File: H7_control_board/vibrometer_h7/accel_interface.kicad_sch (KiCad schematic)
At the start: 0 parts

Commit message: added cubeIDE projects
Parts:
- added C301, C302: 100n, symbol Device:C
- added D301: LED, symbol Device:LED
- added J301, J302: Conn_01x08_Socket, symbol Connector:Conn_01x08_Socket
- added R302: 0R, symbol Device:R_Small_US
- added R?: R, symbol Device:R_Small_US
- added XL1: LSM6DS3, Package_LGA:LGA-14_3x2.5mm_P0.5mm_LayoutBorder3x4y, symbol Sensor_Motion:LSM6DS3
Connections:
- new net: D301.1 (K), R?.1
- new net: D301.2 (A), R302.2
- new net +3V3: C301.1, C302.1, J302.8 (Pin_8), R302.1, XL1.5 (VDDIO), XL1.8 (VDD)
- new net GND: C301.2, C302.2, J302.1 (Pin_1), R?.2, XL1.6 (GND), XL1.7 (GND)
- new net SPI_3V3: J301.8 (Pin_8)
- new net SPI_CS: J301.2 (Pin_2), J302.2 (Pin_2), XL1.12 (CS)
- new net SPI_GND: J301.1 (Pin_1)
- new net SPI_INT1: J301.7 (Pin_7), J302.7 (Pin_7), XL1.4 (INT1)
- new net SPI_INT2: J301.6 (Pin_6), J302.6 (Pin_6), XL1.9 (INT2)
- new net SPI_MISO: J301.5 (Pin_5), J302.5 (Pin_5), XL1.1 (SDO/SA0)
- new net SPI_MOSI: J301.4 (Pin_4), J302.4 (Pin_4), XL1.14 (SDA)
- new net SPI_SCLK: J301.3 (Pin_3), J302.3 (Pin_3), XL1.13 (SCL)
- no-connect marks 0 -> 2

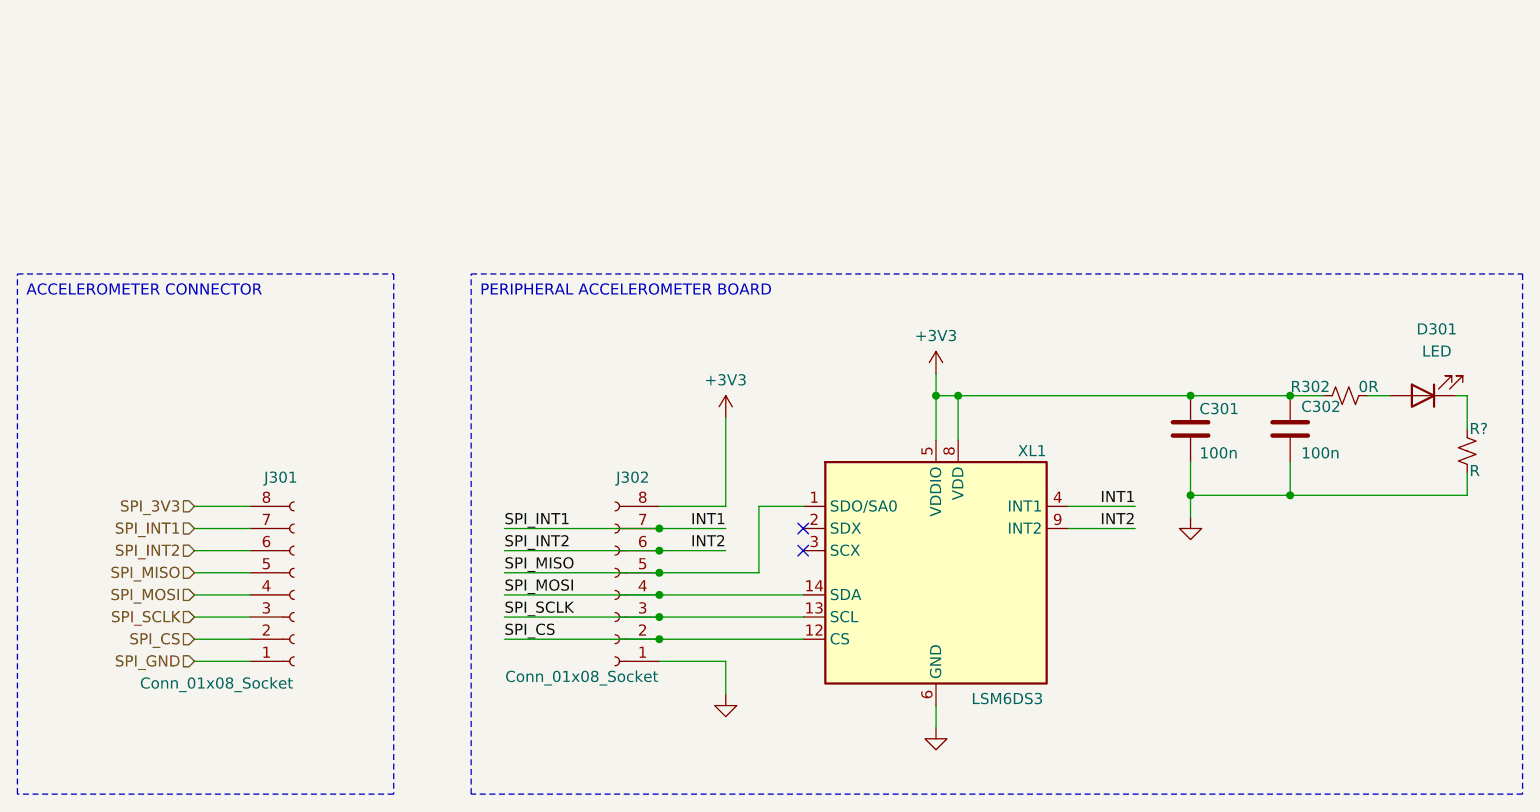
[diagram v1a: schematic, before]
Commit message: added bus notation to kicad schematic
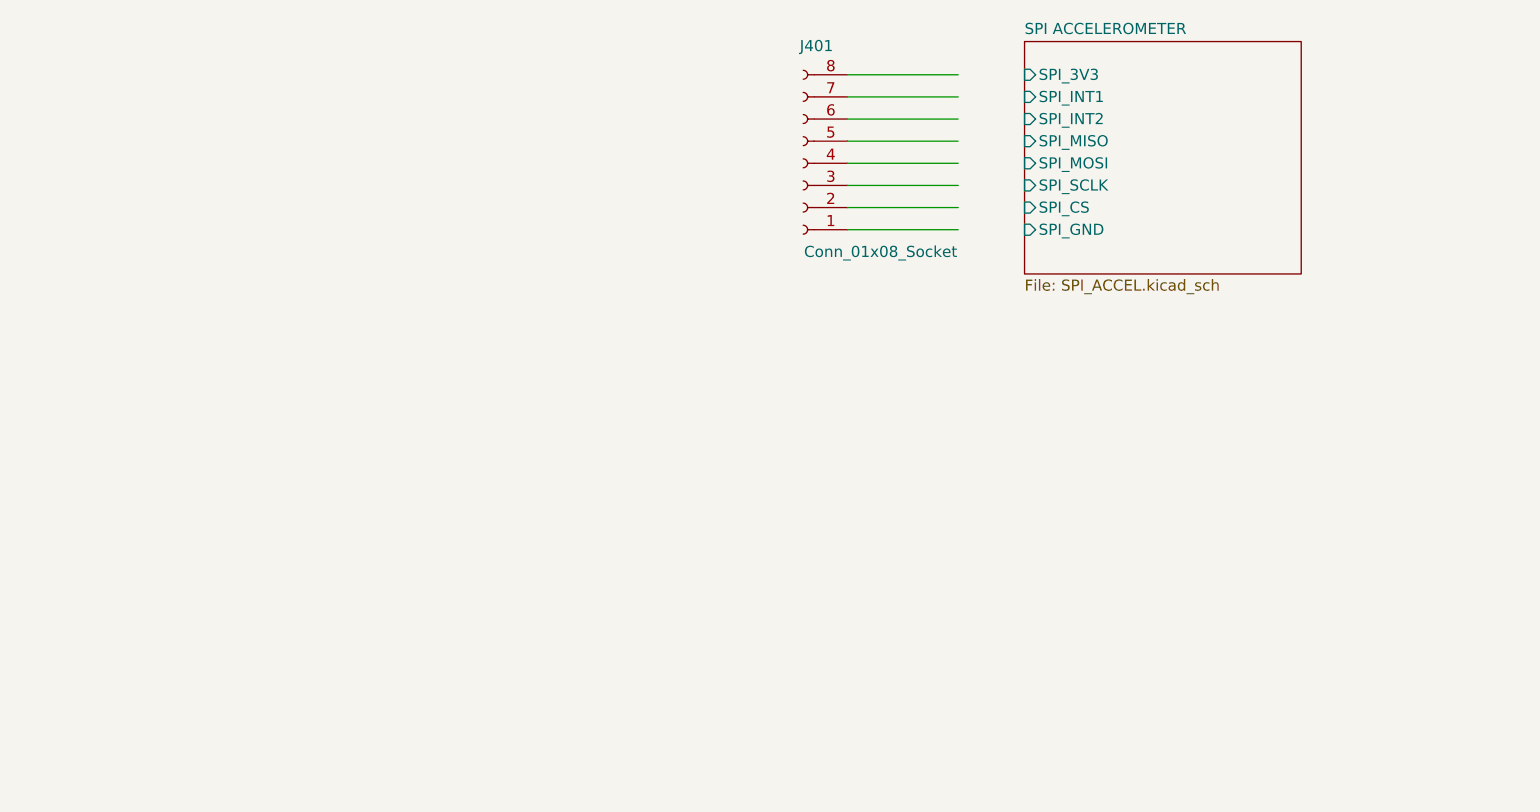
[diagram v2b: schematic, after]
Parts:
- removed C301, C302: 100n, symbol Device:C
- removed D301: LED, symbol Device:LED
- removed J301, J302: Conn_01x08_Socket, symbol Connector:Conn_01x08_Socket
- removed R302: 0R, symbol Device:R_Small_US
- removed R?: R, symbol Device:R_Small_US
- removed XL1: LSM6DS3, Package_LGA:LGA-14_3x2.5mm_P0.5mm_LayoutBorder3x4y, symbol Sensor_Motion:LSM6DS3
- added J401: Conn_01x08_Socket, symbol Connector:Conn_01x08_Socket
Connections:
- no-connect marks 2 -> 0
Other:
- added sheet SPI ACCELEROMETER (SPI_ACCEL.kicad_sch)

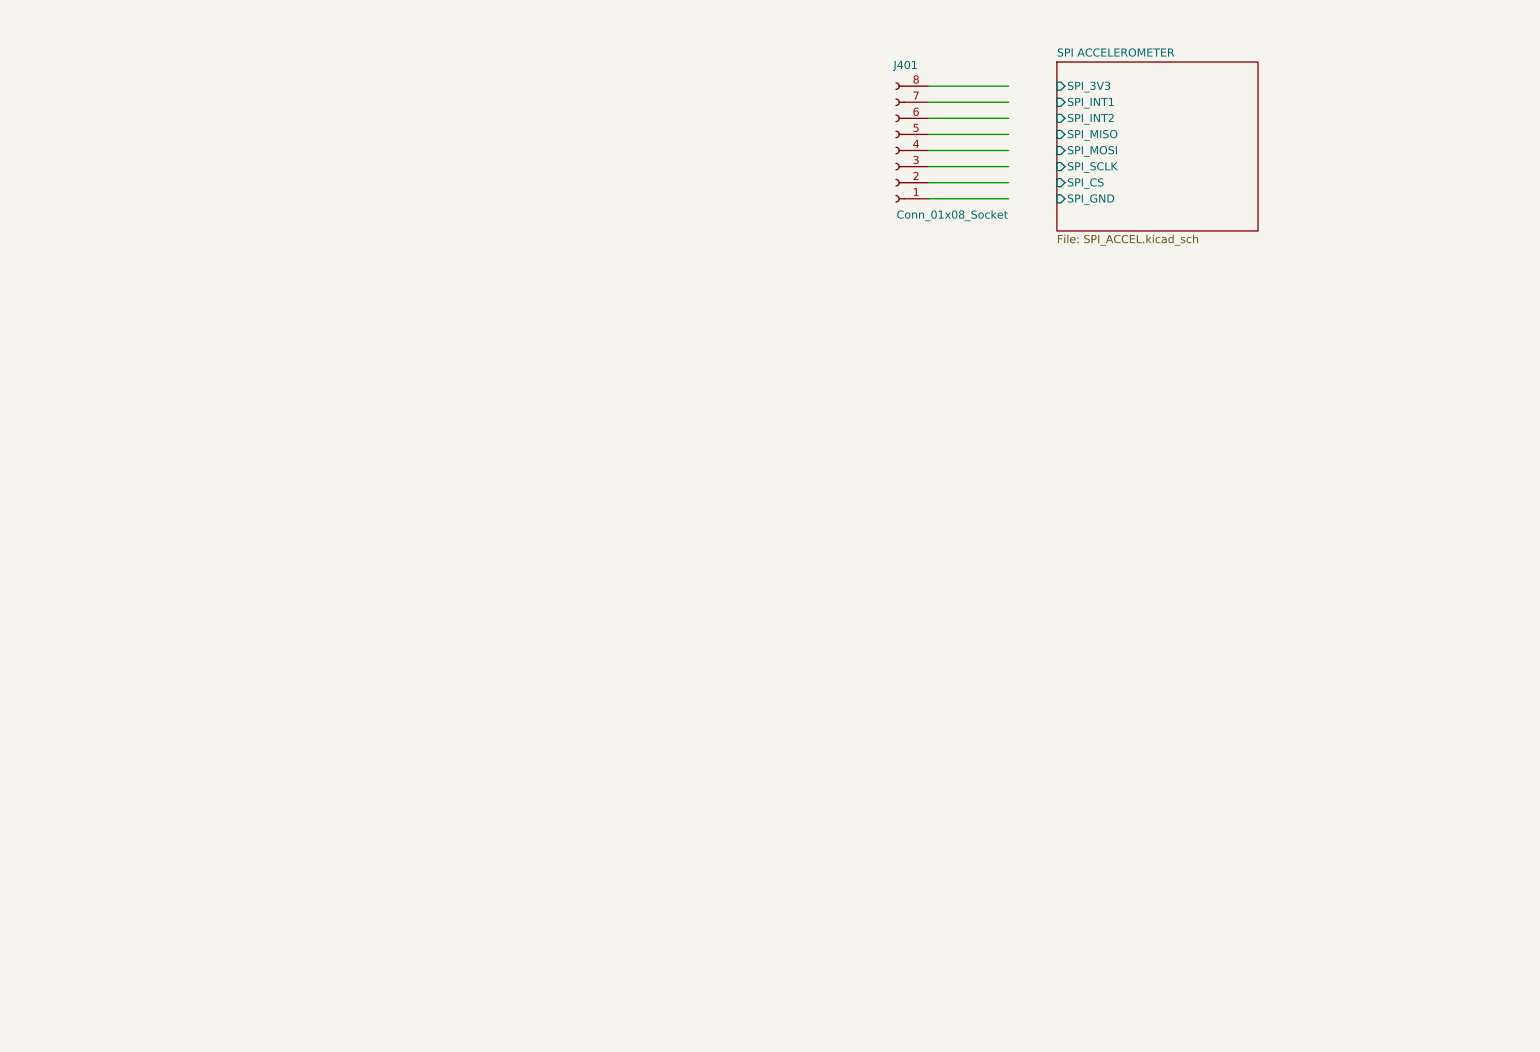
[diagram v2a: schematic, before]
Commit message: added UI leds to schematic
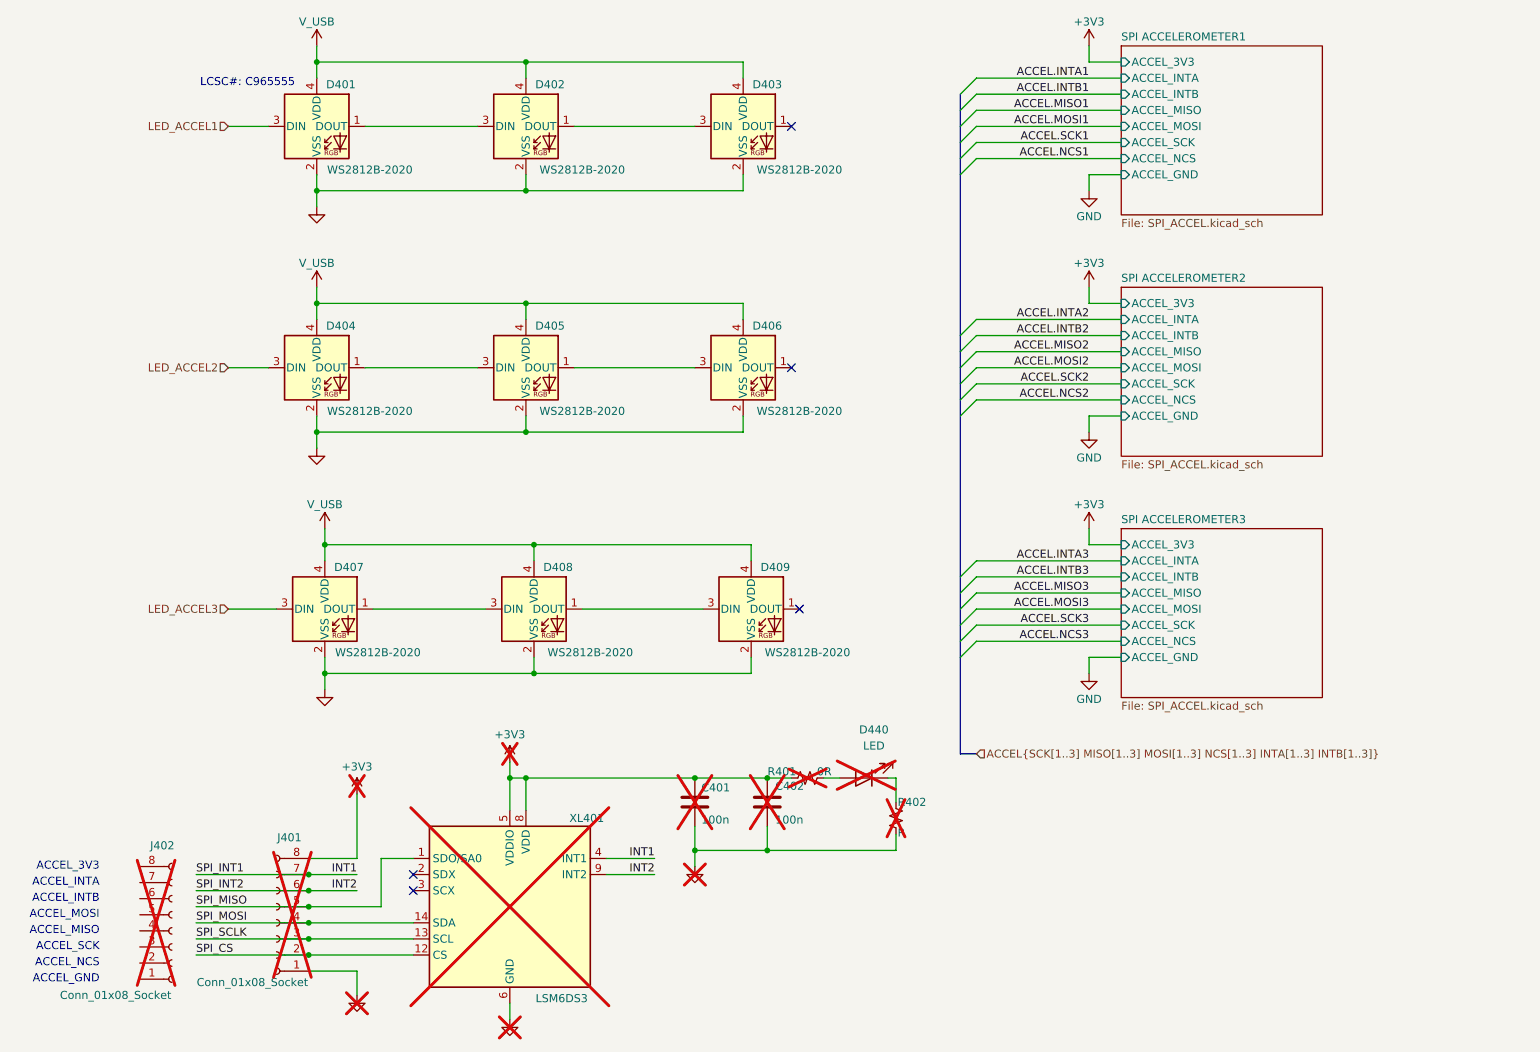
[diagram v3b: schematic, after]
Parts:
- added C401, C402: 100n, symbol Device:C
- added D401, D402, D403, D404, D405, D406, D407, D408, D409: WS2812B-2020, LED_SMD:LED_WS2812B-2020_PLCC4_2.0x2.0mm, symbol LED:WS2812B-2020
- added D440: LED, symbol Device:LED
- added J402: Conn_01x08_Socket, symbol Connector:Conn_01x08_Socket
- added R401: 0R, symbol Device:R_Small_US
- added R402: R, symbol Device:R_Small_US
- added XL401: LSM6DS3, Package_LGA:LGA-14_3x2.5mm_P0.5mm_LayoutBorder3x4y, symbol Sensor_Motion:LSM6DS3
- J401: now not fitted
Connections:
- net GND: now reaches J401.1 (Pin_1)
- net GND: now also C401.2, C402.2, D401.2 (VSS), D402.2 (VSS), D403.2 (VSS), D404.2 (VSS), D405.2 (VSS), D406.2 (VSS), D407.2 (VSS), D408.2 (VSS), D409.2 (VSS), R402.2, XL401.6 (GND), XL401.7 (GND)
- net SPI_CS: now reaches J401.2 (Pin_2)
- net SPI_CS: now also XL401.12 (CS)
- net SPI_SCLK: now reaches J401.3 (Pin_3)
- net SPI_SCLK: now also XL401.13 (SCL)
- net SPI_MOSI: now reaches J401.4 (Pin_4)
- net SPI_MOSI: now also XL401.14 (SDA)
- net SPI_MISO: now reaches J401.5 (Pin_5)
- net SPI_MISO: now also XL401.1 (SDO/SA0)
- net INT2: now reaches J401.6 (Pin_6)
- net INT2: now also XL401.9 (INT2)
- net INT1: now reaches J401.7 (Pin_7)
- net INT1: now also XL401.4 (INT1)
- net +3V3: now reaches J401.8 (Pin_8)
- net +3V3: now also C401.1, C402.1, R401.1, XL401.5 (VDDIO), XL401.8 (VDD)
- new net: D402.1 (DOUT), D403.3 (DIN)
- new net: D401.1 (DOUT), D402.3 (DIN)
- new net: D405.1 (DOUT), D406.3 (DIN)
- new net: D440.1 (K), R402.1
- new net: D440.2 (A), R401.2
- new net: D408.1 (DOUT), D409.3 (DIN)
- new net: D407.1 (DOUT), D408.3 (DIN)
- new net: D404.1 (DOUT), D405.3 (DIN)
- new net LED_ACCEL1: D401.3 (DIN)
- new net LED_ACCEL2: D404.3 (DIN)
- new net LED_ACCEL3: D407.3 (DIN)
- new net V_USB: D401.4 (VDD), D402.4 (VDD), D403.4 (VDD), D404.4 (VDD), D405.4 (VDD), D406.4 (VDD), D407.4 (VDD), D408.4 (VDD), D409.4 (VDD)
- no-connect marks 0 -> 5
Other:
- sheet SPI ACCELEROMETER renamed SPI ACCELEROMETER1
- added sheet SPI ACCELEROMETER2 (SPI_ACCEL.kicad_sch)
- added sheet SPI ACCELEROMETER3 (SPI_ACCEL.kicad_sch)
- sheet SPI ACCELEROMETER1 ports: added ACCEL_3V3, ACCEL_GND, ACCEL_INTA, ACCEL_INTB, ACCEL_MISO, ACCEL_MOSI, ACCEL_NCS, ACCEL_SCK; removed SPI_3V3, SPI_CS, SPI_GND, SPI_INT1, SPI_INT2, SPI_MISO, SPI_MOSI, SPI_SCLK
- note added: "ACCEL_3V3"
- note added: "ACCEL_GND"
- note added: "ACCEL_INTA"
- note added: "ACCEL_INTB"
- note added: "ACCEL_MISO"
- note added: "ACCEL_MOSI"
- note added: "ACCEL_NCS"
- note added: "ACCEL_SCK"
- note added: "LCSC#: C965555"

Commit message: working on getting ERC to run... almost there!
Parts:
- removed C401, C402: 100n, symbol Device:C
- removed D440: LED, symbol Device:LED
- removed J401, J402: Conn_01x08_Socket, symbol Connector:Conn_01x08_Socket
- removed R401: 0R, symbol Device:R_Small_US
- removed R402: R, symbol Device:R_Small_US
- removed XL401: LSM6DS3, Package_LGA:LGA-14_3x2.5mm_P0.5mm_LayoutBorder3x4y, symbol Sensor_Motion:LSM6DS3
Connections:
- no-connect marks 5 -> 3
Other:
- note removed: "ACCEL_3V3"
- note removed: "ACCEL_GND"
- note removed: "ACCEL_INTA"
- note removed: "ACCEL_INTB"
- note removed: "ACCEL_MISO"
- note removed: "ACCEL_MOSI"
- note removed: "ACCEL_NCS"
- note removed: "ACCEL_SCK"

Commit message: worked on audio output stuff, cleaned schematic
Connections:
- net LED_ACCEL2 is gone; now on an unnamed net: D404.3 (DIN)
- net LED_ACCEL3 is gone; now on an unnamed net: D407.3 (DIN)
- net LED_ACCEL1 renamed LED_ACCEL
- net V_USB renamed +5V
- no-connect marks 3 -> 1

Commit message: started part selection
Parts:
- D401, D402, D403, D404, D405, D406, D407, D408, D409: LCSC (none) -> C965555
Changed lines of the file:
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@@
+			)
+		)
+		(property "LCSC" "C965555"
+			(at 96.52 50.8 0)
+			(effects
+				(font
+					(size 1.27 1.27)
+				)
+				(hide yes)
 			)
 		)
@@
 		)
 		(property "Description" "RGB LED with integrated controller, 2.0 x 2.0 mm, 12 mA"
+			(at 130.81 88.9 0)
+			(effects
+				(font
+					(size 1.27 1.27)
+				)
+				(hide yes)
+			)
+		)
+		(property "LCSC" "C965555"
 			(at 130.81 88.9 0)
 			(effects
@@
 			)
 		)
+		(property "LCSC" "C965555"
+			(at 97.79 127 0)
+			(effects
+				(font
+					(size 1.27 1.27)
+				)
+				(hide yes)
+			)
+		)
 		(pin "2"
 		)
@@
 			)
 		)
+		(property "LCSC" "C965555"
+			(at 130.81 50.8 0)
+			(effects
+				(font
+					(size 1.27 1.27)
+				)
+				(hide yes)
+			)
+		)
 		(pin "2"
 		)
@@
 			)
 		)
+		(property "LCSC" "C965555"
+			(at 63.5 50.8 0)
+			(effects
+				(font
+					(size 1.27 1.27)
+				)
+				(hide yes)
+			)
+		)
 		(pin "2"
 		)
@@
 			)
 		)
+		(property "LCSC" "C965555"
+			(at 132.08 127 0)
+			(effects
+				(font
+					(size 1.27 1.27)
+				)
+				(hide yes)
+			)
+		)
 		(pin "2"
 		)
@@
 		)
 		(property "Description" "RGB LED with integrated controller, 2.0 x 2.0 mm, 12 mA"
+			(at 64.77 127 0)
+			(effects
+				(font
+					(size 1.27 1.27)
+				)
+				(hide yes)
+			)
+		)
+		(property "LCSC" "C965555"
 			(at 64.77 127 0)
 			(effects
@@
 			)
 		)
+		(property "LCSC" "C965555"
+			(at 96.52 88.9 0)
+			(effects
+				(font
+					(size 1.27 1.27)
+				)
+				(hide yes)
+			)
+		)
 		(pin "2"
 		)
@@
 			(at 63.5 88.9 0)
 			(effects
+				(font
+					(size 1.27 1.27)
+				)
+				(hide yes)
+			)
+		)
+		(property "LCSC" "C965555"
+			(at 63.5 88.9 0)
+			(effects

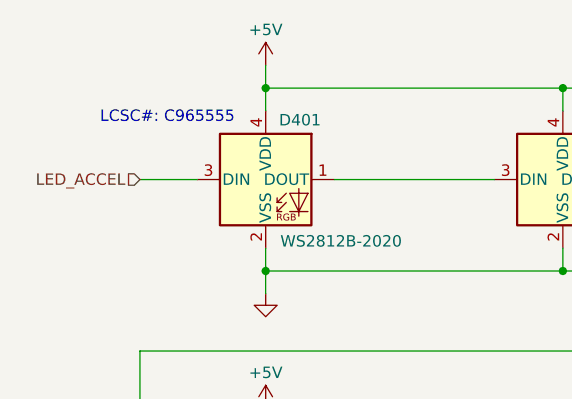
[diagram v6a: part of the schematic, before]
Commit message: part selection for audio, schematic cleanup
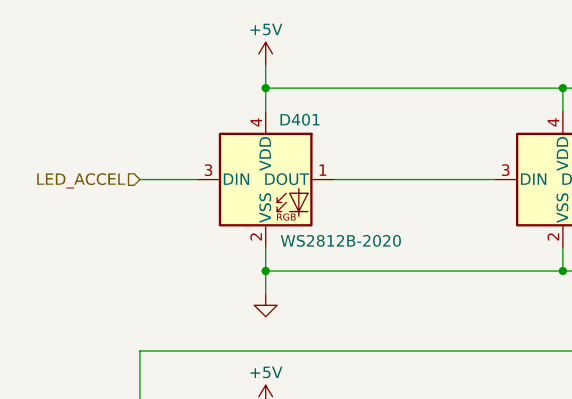
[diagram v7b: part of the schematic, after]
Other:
- note removed: "LCSC#: C965555"
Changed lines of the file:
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@@
-		)
-	)
-	(text "LCSC#: C965555"
-		(exclude_from_sim no)
-		(at 52.578 43.942 0)
-		(effects
-			(font
-				(size 1.27 1.27)
-			)
 		)
 	)
